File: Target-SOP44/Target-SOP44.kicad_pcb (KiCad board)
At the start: 2 copper layers, 28.4 x 15.2 mm, 3 parts, among them J1 FFC-50, J2 SOP44-Castellations, J3 TRESET

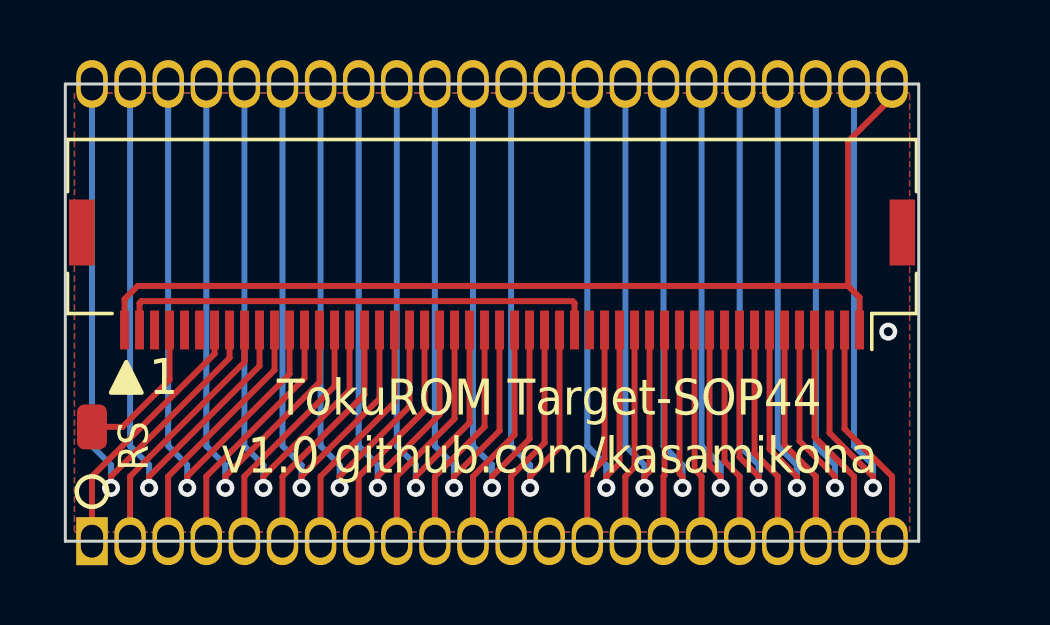
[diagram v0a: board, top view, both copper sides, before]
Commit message: Slightly enlarge Target-SOP44 outline for corner quality
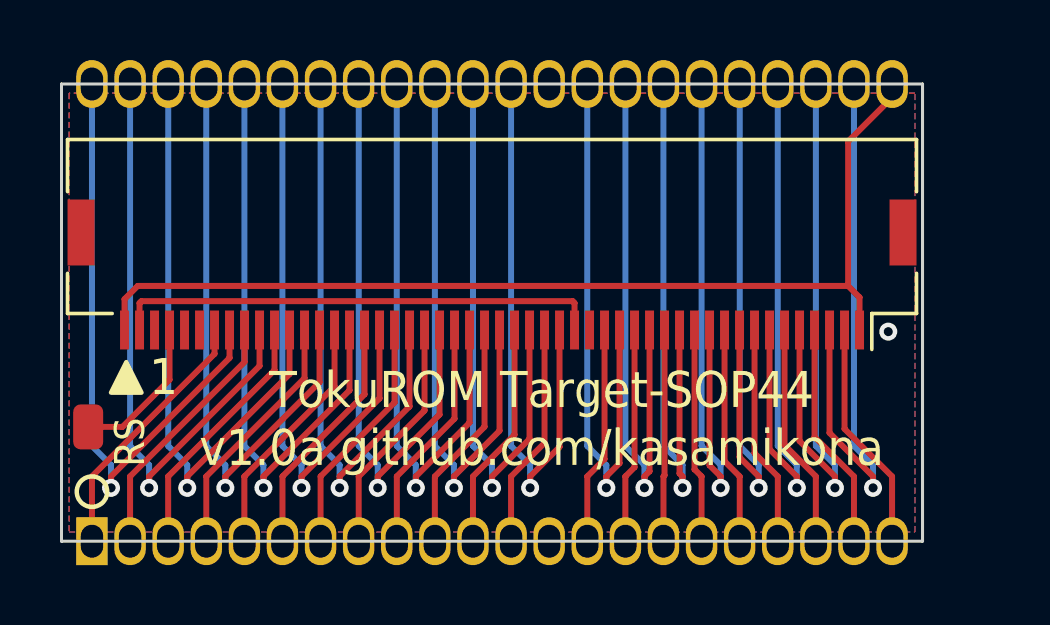
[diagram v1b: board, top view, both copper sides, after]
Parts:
- moved J3 0.13 mm to (16.4, 26.7)
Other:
- board size 28.4 x 15.2 mm -> 28.7 x 15.2 mm
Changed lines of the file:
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@@
   (title_block
     (title "TokuROM Target-SOP44")
-    (rev "1.0")
+    (rev "1.0a")
     (company "github.com/kasamikona/TokuROM")
   )
@@
   )
   (footprint "Tokurom-Parts:SolderPad-Small_Custom" (layer "F.Cu")
-    (at 16.51 26.67)
+    (at 16.383 26.67)
     (descr "Wire Pad, Square, SMD Pad,  1mm x 2mm,")
     (tags "MesurementPoint Square SMDPad 1mmx2mm ")
@@
     (pad "50" smd rect (at 12.25 -1.85 180) (size 0.3 1.3) (layers "F.Cu" "F.Paste" "F.Mask")
       (net 39 "/VCC") (pinfunction "Pin_50") (pintype "passive"))
-    (pad "MP" smd rect (at -13.675 1.4 180) (size 0.85 2.2) (layers "F.Cu" "F.Paste" "F.Mask")
+    (pad "MP" smd rect (at -13.7 1.4 180) (size 0.9 2.2) (layers "F.Cu" "F.Paste" "F.Mask")
       (net 21 "/GND") (pinfunction "MountPin") (pintype "passive"))
-    (pad "MP" smd rect (at 13.675 1.4 180) (size 0.85 2.2) (layers "F.Cu" "F.Paste" "F.Mask")
+    (pad "MP" smd rect (at 13.7 1.4 180) (size 0.9 2.2) (layers "F.Cu" "F.Paste" "F.Mask")
       (net 21 "/GND") (pinfunction "MountPin") (pintype "passive"))
     (model "${KIPRJMOD}/../Tokurom-Parts.pretty/FFC-50.stp"
@@
   (gr_circle (center 16.51 28.829) (end 17.018 28.829)
     (stroke (width 0.15) (type default)) (fill none) (layer "F.SilkS"))
-  (gr_line (start 15.621 30.48) (end 15.621 15.24)
+  (gr_line (start 15.494 30.48) (end 15.494 15.24)
     (stroke (width 0.1) (type default)) (layer "Edge.Cuts"))
-  (gr_line (start 15.621 15.24) (end 44.069 15.24)
+  (gr_line (start 15.494 15.24) (end 44.196 15.24)
     (stroke (width 0.1) (type default)) (layer "Edge.Cuts"))
-  (gr_line (start 44.069 15.24) (end 44.069 30.48)
+  (gr_line (start 44.196 15.24) (end 44.196 30.48)
     (stroke (width 0.1) (type default)) (layer "Edge.Cuts"))
-  (gr_line (start 44.069 30.48) (end 15.621 30.48)
+  (gr_line (start 44.196 30.48) (end 15.494 30.48)
     (stroke (width 0.1) (type default)) (layer "Edge.Cuts"))
   (gr_text "THIS SIDE CHIP BOTTOM\n\nTokuROM Target-SOP44 v${REVISION}\ngithub.com/kasamikona" (at 29.845 22.86) (layer "B.SilkS")
@@
     (effects (font (size 1.2 1.1) (thickness 0.15)) (justify left))
   )
-  (gr_text "RS" (at 17.907 27.305 90) (layer "F.SilkS")
+  (gr_text "RS" (at 17.78 27.178 90) (layer "F.SilkS")
     (effects (font (size 1 0.9) (thickness 0.125)))
   )
-  (gr_text "TokuROM Target-SOP44\nv${REVISION} github.com/kasamikona" (at 31.75 26.67) (layer "F.SilkS")
+  (gr_text "TokuROM Target-SOP44\nv${REVISION} github.com/kasamikona" (at 31.496 26.416) (layer "F.SilkS")
     (effects (font (size 1.2 1.1) (thickness 0.15)))
   )
@@
   (segment (start 19.095 25.101) (end 19.095 23.44) (width 0.2) (layer "F.Cu") (net 47))
   (segment (start 17.526 26.67) (end 19.095 25.101) (width 0.2) (layer "F.Cu") (net 47))
-  (segment (start 16.51 26.67) (end 17.526 26.67) (width 0.2) (layer "F.Cu") (net 47))
+  (segment (start 16.383 26.67) (end 17.526 26.67) (width 0.2) (layer "F.Cu") (net 47))
   (zone (net 0) (net_name "") (layer "F.Cu") (hatch edge 0.5)
     (connect_pads (clearance 0))
@@
     (polygon
       (pts
-        (xy 15.9258 30.1752)
-        (xy 43.7642 30.1752)
-        (xy 43.7642 15.5448)
-        (xy 15.9258 15.5448)
+        (xy 15.748 30.1752)
+        (xy 43.942 30.1752)
+        (xy 43.942 15.5448)
+        (xy 15.748 15.5448)
       )
     )
